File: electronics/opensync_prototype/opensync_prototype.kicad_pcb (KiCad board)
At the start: 4 copper layers, 160 x 100 mm, 107 parts, among them J1 61400416121, J10 61611042121502, J11 61611042121502, J2 61611042121502, J4 61611042121502, J5 61611042121502, J6 61611042121502, J7 61611042121502, J8 61611042121502, J9 61611042121502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

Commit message: PCB rework
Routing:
- added copper zone on F.Cu, net +1V1
- added copper zone on In2.Cu, net +5V
- added copper zone on B.Cu, net GND
- added copper zone on In1.Cu, net GND
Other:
- board text added: "LED Indicators"
- board text added: "Safety Interlock"
- board text removed: "The Following Features Will Be Inc. Here - Safety Interlock - Power LED - Error LED"
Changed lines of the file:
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@@
 		(tags "capacitor")
 		(property "Reference" "C23"
-			(at 2.25 -1.16 0)
+			(at 1.7 1.4 0)
 			(layer "F.SilkS")
 			(effects
@@
 		(tags "capacitor")
 		(property "Reference" "C5"
-			(at 0 -1.85 0)
+			(at 0 1.935 0)
 			(layer "F.SilkS")
 			(effects
@@
 		(tags "capacitor")
 		(property "Reference" "C11"
-			(at 0 -1.16 0)
+			(at 1.285 1.7 0)
 			(layer "F.SilkS")
 			(effects
@@
 		(layer "Edge.Cuts")
 	)
-	(gr_text "OpenPIV © 2025\nOpenSync v0.1"
-		(at 68.2 62.8 0)
+	(gr_text "LED\nIndicators"
+		(at 209.2 117.4 0)
 		(layer "F.SilkS")
 		(effects
 			(font
-				(size 4 4)
-				(thickness 0.8)
+				(size 1.5 1.5)
+				(thickness 0.3)
 				(bold yes)
 			)
@@
 		)
 	)
-	(gr_text "The Following Features Will Be Inc. Here\n - Safety Interlock\n - Power LED\n - Error LED"
-		(at 174.2 81.8 0)
+	(gr_text "OpenPIV © 2025\nOpenSync v0.1"
+		(at 68.2 62.8 0)
 		(layer "F.SilkS")
 		(effects
 			(font
-				(size 1.5 1.5)
-				(thickness 0.3)
+				(size 4 4)
+				(thickness 0.8)
 				(bold yes)
 			)
@@
 		)
 	)
+	(gr_text "Safety\nInterlock"
+		(at 166.8 55.6 0)
+		(layer "F.SilkS")
+		(effects
+			(font
+				(size 1.5 1.5)
+				(thickness 0.3)
+				(bold yes)
+			)
+			(justify left bottom)
+		)
+	)
 	(gr_text "USB"
 		(at 141.5 55.5 0)
@@
 		)
 	)
+	(zone
+		(net 6)
+		(net_name "+1V1")
+		(layer "F.Cu")
+		(hatch edge 0.5)
+		(priority 3)
+		(connect_pads
+			(clearance 0.2)
+		)
+		(min_thickness 0.2)
+		(filled_areas_thickness no)
+		(fill
+			(thermal_gap 0.3)
+			(thermal_bridge_width 0.3)
+		)
+		(polygon
+			(pts
+				(xy 128.2 91.6) (xy 134.4 91.6) (xy 134.4 97.6) (xy 128.2 97.6)
+			)
+		)
+	)
+	(zone
+		(net 2)
+		(net_name "GND")
+		(layer "B.Cu")
+		(hatch edge 0.5)
+		(priority 2)
+		(connect_pads
+			(clearance 1)
+		)
+		(min_thickness 0.2)
+		(filled_areas_thickness no)
+		(fill
+			(thermal_gap 0.2)
+			(thermal_bridge_width 0.2)
+		)
+		(polygon
+			(pts
+				(xy 62 45) (xy 222 45) (xy 222 145) (xy 62 145)
+			)
+		)
+	)
+	(zone
+		(net 2)
+		(net_name "GND")
+		(layer "In1.Cu")
+		(hatch edge 0.5)
+		(connect_pads
+			(clearance 1)
+		)
+		(min_thickness 0.2)
+		(filled_areas_thickness no)
+		(fill
+			(thermal_gap 0.2)
+			(thermal_bridge_width 0.2)
+		)
+		(polygon
+			(pts
+				(xy 62 45) (xy 222 45) (xy 222 145) (xy 62 145)
+			)
+		)
+	)
+	(zone
+		(net 10)
+		(net_name "+5V")
+		(layer "In2.Cu")
+		(hatch edge 0.5)
+		(priority 1)
+		(connect_pads
+			(clearance 1)
+		)
+		(min_thickness 0.2)
+		(filled_areas_thickness no)
+		(fill
+			(thermal_gap 0.2)
+			(thermal_bridge_width 0.2)
+		)
+		(polygon
+			(pts
+				(xy 62 45) (xy 222 45) (xy 222 145) (xy 62 145)
+			)
+		)
+	)

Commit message: PCB trace routes
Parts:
- moved J11 105.0 mm to (202.0, 140.0)
- moved J4 105.0 mm to (97.0, 140.0)
- moved J10 75.0 mm to (187.0, 140.0)
- moved J5 75.0 mm to (112.0, 140.0)
- moved J6 45.0 mm to (127.0, 140.0)
- moved J9 45.0 mm to (172.0, 140.0)
- moved J7 15.0 mm to (142.0, 140.0)
- moved J8 15.0 mm to (157.0, 140.0)
- moved C5 13.3 mm to (136.2, 88.1)
- moved C1 0.58 mm to (134.0, 88.0)
- moved C4 0.58 mm to (134.0, 87.1)
- moved L1 0.58 mm to (134.0, 85.5)
- moved C10 0.29 mm to (129.7, 102.9)
- moved R1 0.29 mm to (136.2, 86.2)
- moved R2 0.29 mm to (131.2, 102.9), turned to 90 degrees
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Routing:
- net +3V3: track 0.00 -> 19.8 mm
- net /Microcontroller and Ext. Clock/XIN: track 0.00 -> 10.9 mm
- net /Microcontroller and Ext. Clock/TRIGGER_1: track 0.00 -> 6.61 mm
- net /Microcontroller and Ext. Clock/CLOCK_3: track 0.00 -> 5.53 mm
- net Net-(C3-Pad2): track 0.00 -> 5.34 mm
- net /Microcontroller and Ext. Clock/CLOCK_1: track 0.00 -> 5.16 mm
- net /Microcontroller and Ext. Clock/CLOCK_2: track 0.00 -> 4.90 mm
- net Net-(U9-B): track 0.00 -> 4.65 mm
- net Net-(U8-B): track 0.00 -> 4.65 mm
- net Net-(U12-B): track 0.00 -> 4.65 mm
- net Net-(U11-B): track 0.00 -> 4.65 mm
- net Net-(U10-B): track 0.00 -> 4.65 mm
- net Net-(U7-B): track 0.00 -> 4.65 mm
- net Net-(U6-B): track 0.00 -> 4.65 mm
- net Net-(U5-B): track 0.00 -> 4.65 mm
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- added copper zone on F.Cu, net GND

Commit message: Hotel backup
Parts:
- moved R3 1.58 mm to (90.0, 101.0)
- moved SW2 1.58 mm to (96.0, 100.0)
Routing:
- net /Microcontroller and Ext. Clock/OUTPUT_8: track 1.66 -> 82.3 mm
- net /Microcontroller and Ext. Clock/OUTPUT_7: track 1.66 -> 67.8 mm
- net /Microcontroller and Ext. Clock/OUTPUT_1: track 1.66 -> 58.4 mm
- net /Microcontroller and Ext. Clock/TRIGGER_1: track 6.61 -> 62.1 mm
- net /Microcontroller and Ext. Clock/OUTPUT_6: track 1.66 -> 53.2 mm
- net /Microcontroller and Ext. Clock/OUTPUT_2: track 1.66 -> 44.1 mm
- net /Microcontroller and Ext. Clock/OUTPUT_5: track 1.66 -> 40.6 mm
- net /Microcontroller and Ext. Clock/OUTPUT_4: track 1.66 -> 34.6 mm
- net /Microcontroller and Ext. Clock/OUTPUT_3: track 1.66 -> 32.2 mm
- net Net-(J2-Pad1): track 0.00 -> 6.49 mm
- net +3V3: track 19.8 -> 23.1 mm
- net Net-(U4-A): track 0.00 -> 2.03 mm

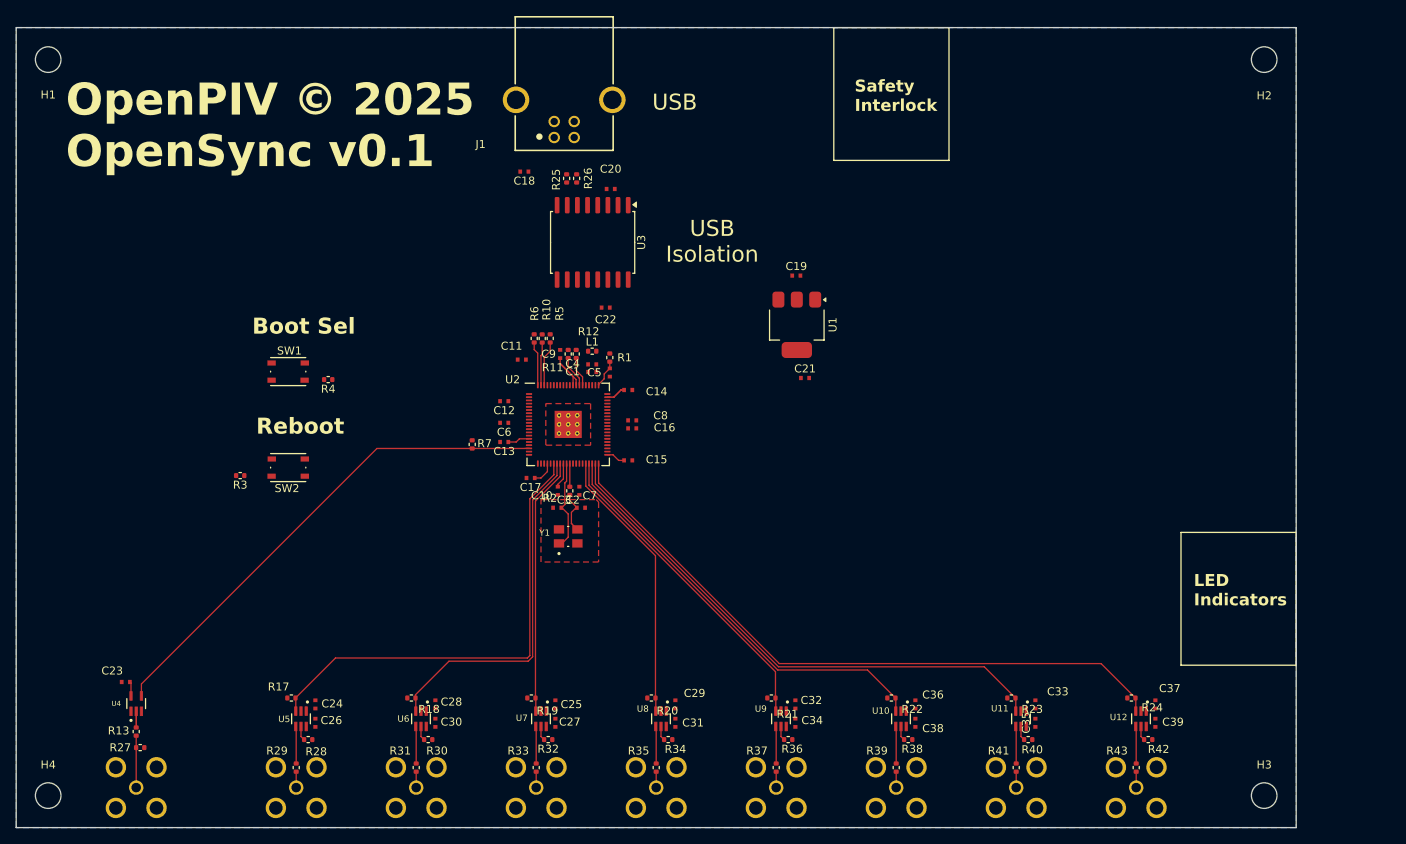
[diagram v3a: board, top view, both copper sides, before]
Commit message: Trace routing and vias
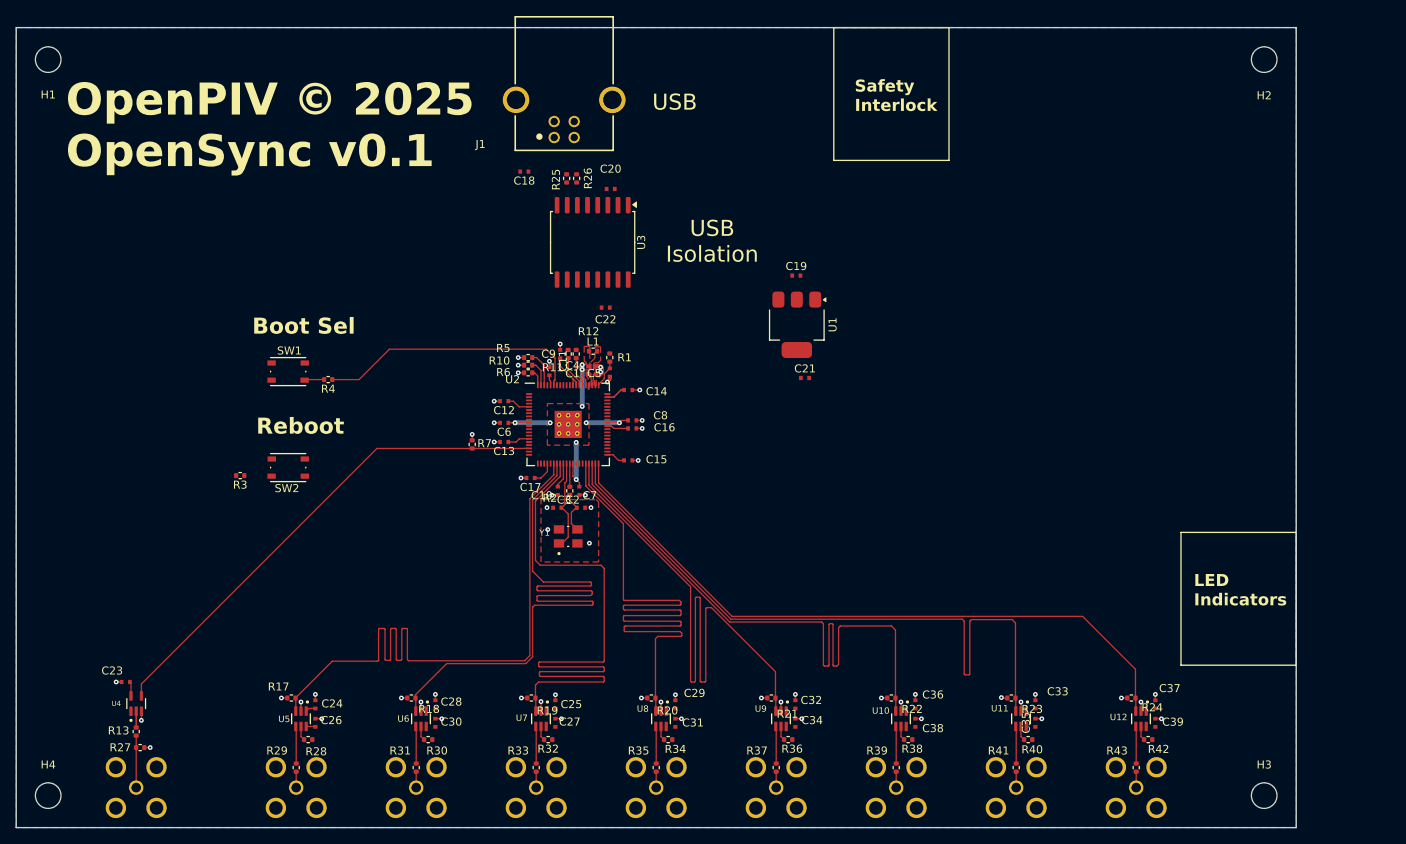
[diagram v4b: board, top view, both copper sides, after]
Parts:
- moved R6 4.36 mm to (126.0, 88.2), turned to 0 degrees
- moved R10 3.77 mm to (126.0, 87.2), turned to 0 degrees
- moved C11 3.74 mm to (128.7, 88.0), turned to 90 degrees
- moved R5 3.65 mm to (126.0, 86.2), turned to 0 degrees
- moved C1 0.25 mm to (134.0, 88.3)
- moved C4 0.25 mm to (134.0, 87.3)
- moved L1 0.11 mm to (134.1, 85.5)
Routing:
- net /Microcontroller and Ext. Clock/OUTPUT_4: track 34.6 -> 85.3 mm
- net /Microcontroller and Ext. Clock/OUTPUT_3: track 32.2 -> 80.7 mm
- net GND: track 0.00 -> 42.4 mm, vias 0 -> 58
- net /Microcontroller and Ext. Clock/OUTPUT_5: track 40.6 -> 81.5 mm
- net /Microcontroller and Ext. Clock/OUTPUT_2: track 44.1 -> 85.0 mm
- net /Microcontroller and Ext. Clock/QSPL_SS: track 0.00 -> 33.3 mm
- net +1V1: track 0.00 -> 30.0 mm, vias 0 -> 9
- net /Microcontroller and Ext. Clock/OUTPUT_6: track 53.2 -> 78.5 mm
- net /Microcontroller and Ext. Clock/OUTPUT_1: track 58.4 -> 81.8 mm
- net /Microcontroller and Ext. Clock/OUTPUT_7: track 67.8 -> 86.7 mm
- net +3V3: track 23.1 -> 28.7 mm
- net /Microcontroller and Ext. Clock/CLOCK_3: track 5.53 -> 2.00 mm
- net Net-(R4-Pad2): track 0.00 -> 2.47 mm
- net /Microcontroller and Ext. Clock/CLOCK_2: track 5.40 -> 3.21 mm
- net /Microcontroller and Ext. Clock/OUTPUT_8: track 82.3 -> 84.4 mm
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- added copper zone on F.Cu, net +3V3
- added copper zone on F.Cu, net /VREG_LX

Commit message: Routed buttons
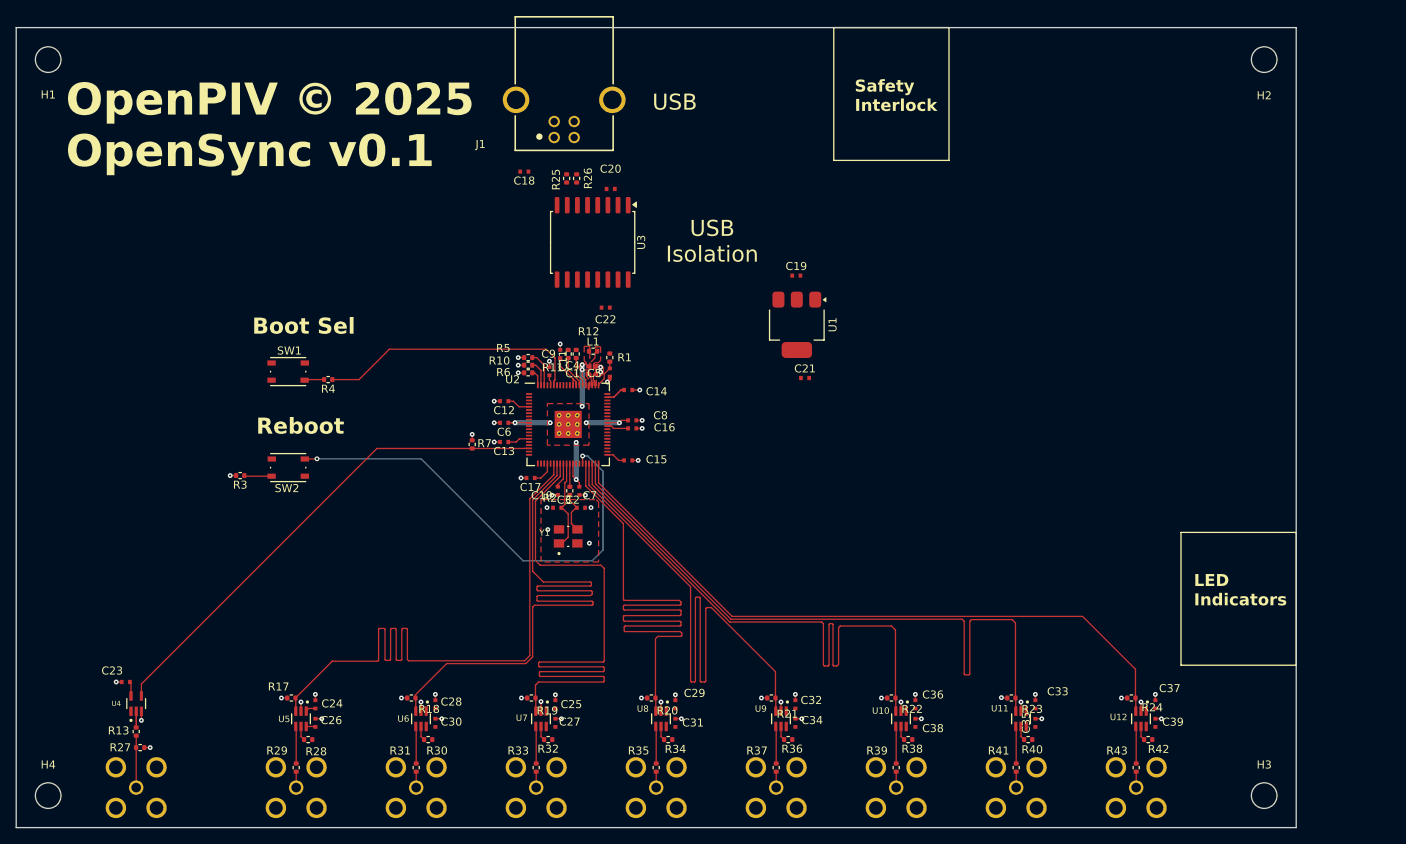
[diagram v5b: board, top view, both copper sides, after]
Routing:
- net /Microcontroller and Ext. Clock/RUN: track 0.00 -> 57.3 mm, vias 0 -> 2
- net Net-(R3-Pad1): track 0.00 -> 3.45 mm
- net GND: track 42.4 -> 43.2 mm, vias 58 -> 59
- removed copper zone on B.Cu, net GND
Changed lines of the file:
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@@
 	)
 	(segment
+		(start 89.49 101)
+		(end 88.75 101)
+		(width 0.15)
+		(layer "F.Cu")
+		(net 2)
+	)
+	(segment
 		(start 119 96.59)
 		(end 119 95.85)
@@
 	)
 	(via micro
+		(at 88.75 101)
+		(size 0.6)
+		(drill 0.25)
+		(layers "F.Cu" "In1.Cu")
+		(net 2)
+	)
+	(via micro
 		(at 127.6 129.25)
 		(size 0.6)
@@
 	)
 	(segment
+		(start 93.925 101.075)
+		(end 90.585 101.075)
+		(width 0.15)
+		(layer "F.Cu")
+		(net 30)
+	)
+	(segment
+		(start 90.585 101.075)
+		(end 90.51 101)
+		(width 0.2)
+		(layer "F.Cu")
+		(net 30)
+	)
+	(segment
 		(start 100.49 89)
 		(end 98.125 89)
@@
 	)
 	(segment
+		(start 99.6 98.9)
+		(end 99.575 98.925)
+		(width 0.15)
+		(layer "F.Cu")
+		(net 55)
+	)
+	(segment
+		(start 99.575 98.925)
+		(end 98.075 98.925)
+		(width 0.15)
+		(layer "F.Cu")
+		(net 55)
+	)
+	(segment
+		(start 132.8 98.55)
+		(end 132.8 99.4965)
+		(width 0.15)
+		(layer "F.Cu")
+		(net 55)
+	)
+	(via
+		(at 99.6 98.9)
+		(size 0.6)
+		(drill 0.3)
+		(layers "F.Cu" "B.Cu")
+		(free yes)
+		(net 55)
+	)
+	(via
+		(at 132.8 98.55)
+		(size 0.6)
+		(drill 0.3)
+		(layers "F.Cu" "B.Cu")
+		(free yes)
+		(net 55)
+	)
+	(segment
+		(start 134 111.65)
+		(end 125.35 111.65)
+		(width 0.15)
+		(layer "B.Cu")
+		(net 55)
+	)
+	(segment
+		(start 133.45 98.55)
+		(end 135.35 100.45)
+		(width 0.15)
+		(layer "B.Cu")
+		(net 55)
+	)
+	(segment
+		(start 112.6 98.9)
+		(end 99.6 98.9)
+		(width 0.15)
+		(layer "B.Cu")
+		(net 55)
+	)
+	(segment
+		(start 135.35 110.3)
+		(end 134 111.65)
+		(width 0.15)
+		(layer "B.Cu")
+		(net 55)
+	)
+	(segment
+		(start 135.35 100.45)
+		(end 135.35 110.3)
+		(width 0.15)
+		(layer "B.Cu")
+		(net 55)
+	)
+	(segment
+		(start 132.8 98.55)
+		(end 133.45 98.55)
+		(width 0.15)
+		(layer "B.Cu")
+		(net 55)
+	)
+	(segment
+		(start 125.35 111.65)
+		(end 112.6 98.9)
+		(width 0.15)
+		(layer "B.Cu")
+		(net 55)
+	)
+	(segment
 		(start 172 136.99)
 		(end 172 132.41)
@@
 			)
 		)
-	)
-	(zone
-		(net 2)
-		(net_name "GND")
-		(layer "B.Cu")
-		(hatch edge 0.5)
-		(priority 2)
-		(connect_pads
-			(clearance 1)
-		)
-		(min_thickness 0.2)
-		(filled_areas_thickness no)
-		(fill
-			(thermal_gap 0.2)
-			(thermal_bridge_width 0.2)
-		)
-		(polygon
-			(pts
-				(xy 62 45) (xy 222 45) (xy 222 145) (xy 62 145)
-			)
-		)

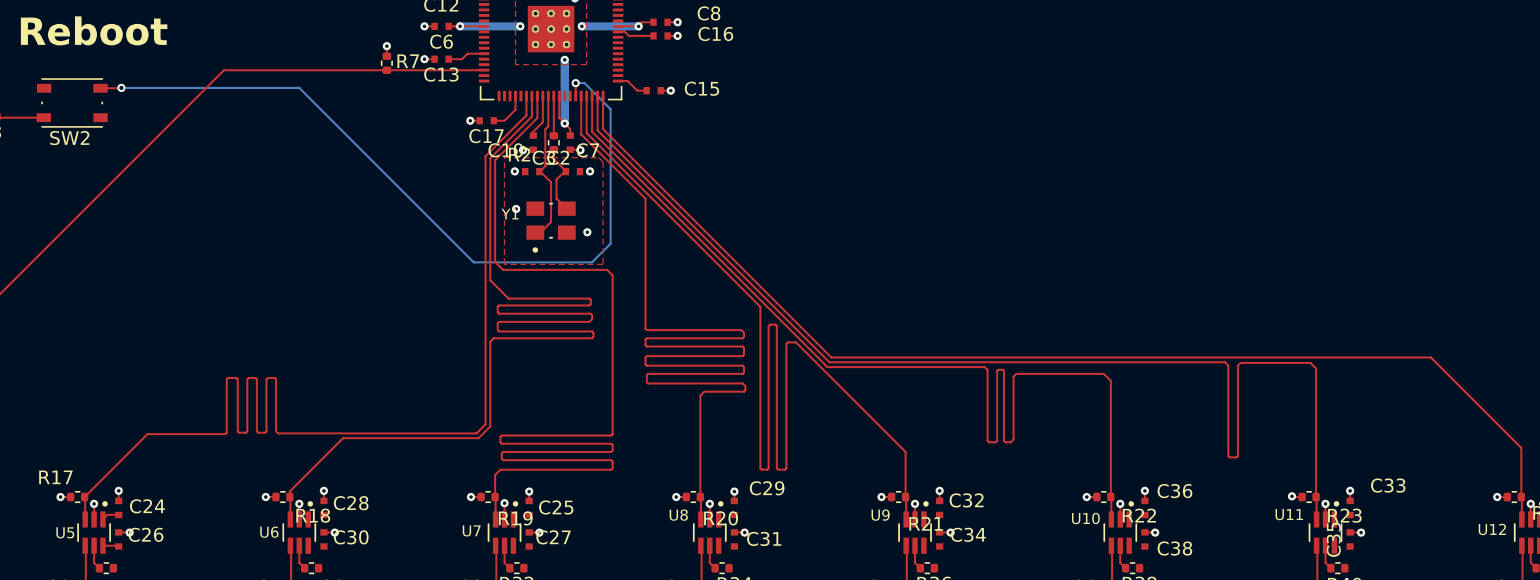
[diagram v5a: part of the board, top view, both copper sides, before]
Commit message: Somewhat tighter trace matching
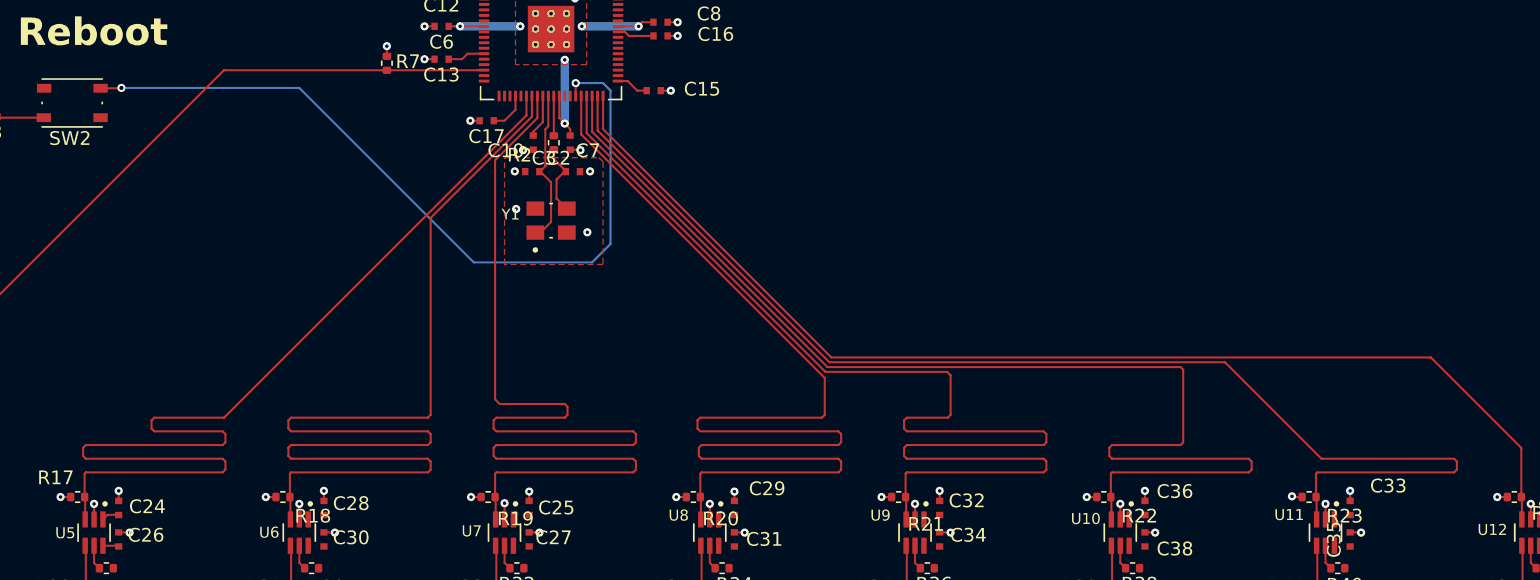
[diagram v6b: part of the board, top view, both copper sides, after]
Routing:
- net /Microcontroller and Ext. Clock/OUTPUT_6: track 78.5 -> 89.4 mm
- net /Microcontroller and Ext. Clock/OUTPUT_5: track 81.5 -> 91.0 mm
- net /Microcontroller and Ext. Clock/OUTPUT_7: track 86.7 -> 89.7 mm
- net /Microcontroller and Ext. Clock/OUTPUT_4: track 85.3 -> 88.0 mm
- net /Microcontroller and Ext. Clock/OUTPUT_3: track 80.7 -> 83.0 mm
- net /Microcontroller and Ext. Clock/OUTPUT_1: track 81.8 -> 80.9 mm
- net /Microcontroller and Ext. Clock/RUN: track 57.3 -> 58.1 mm
